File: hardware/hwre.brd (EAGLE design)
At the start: 71.4 x 62.2 mm, 29 parts

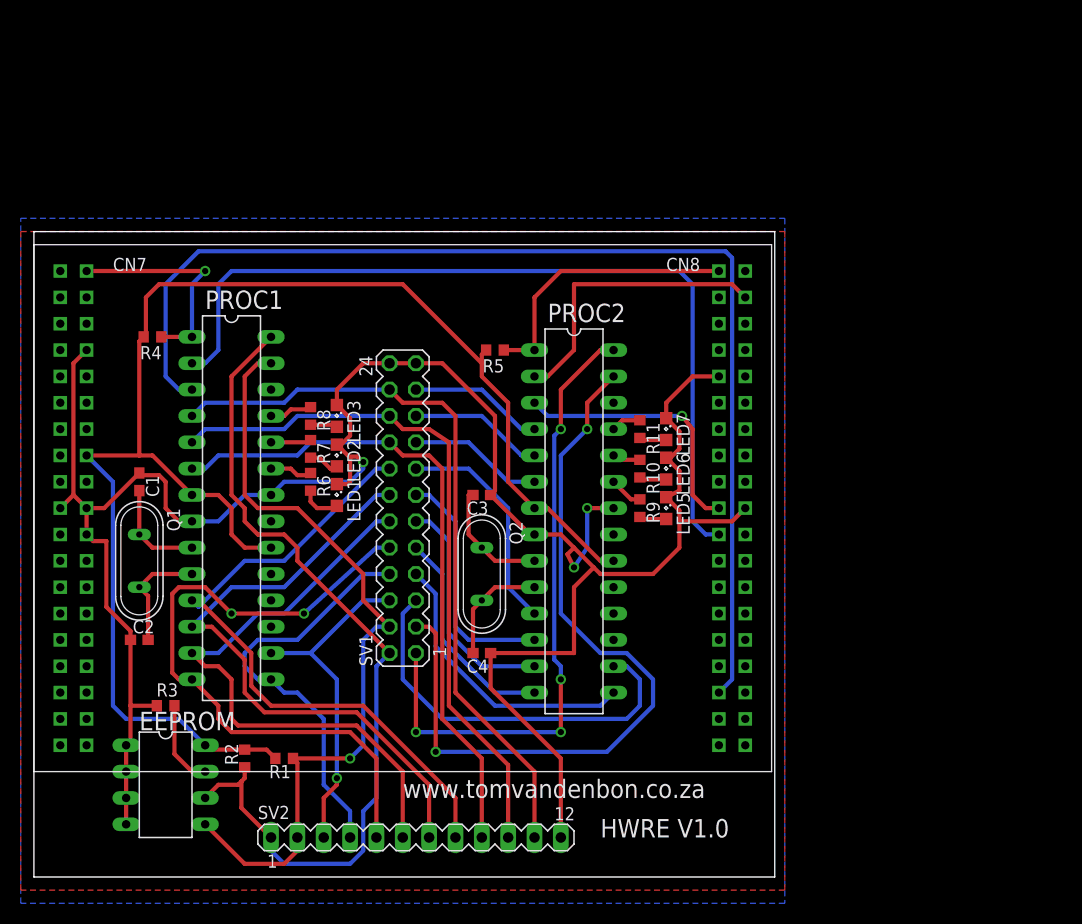
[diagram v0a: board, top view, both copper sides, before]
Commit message: updated pcb to hwre v1.1
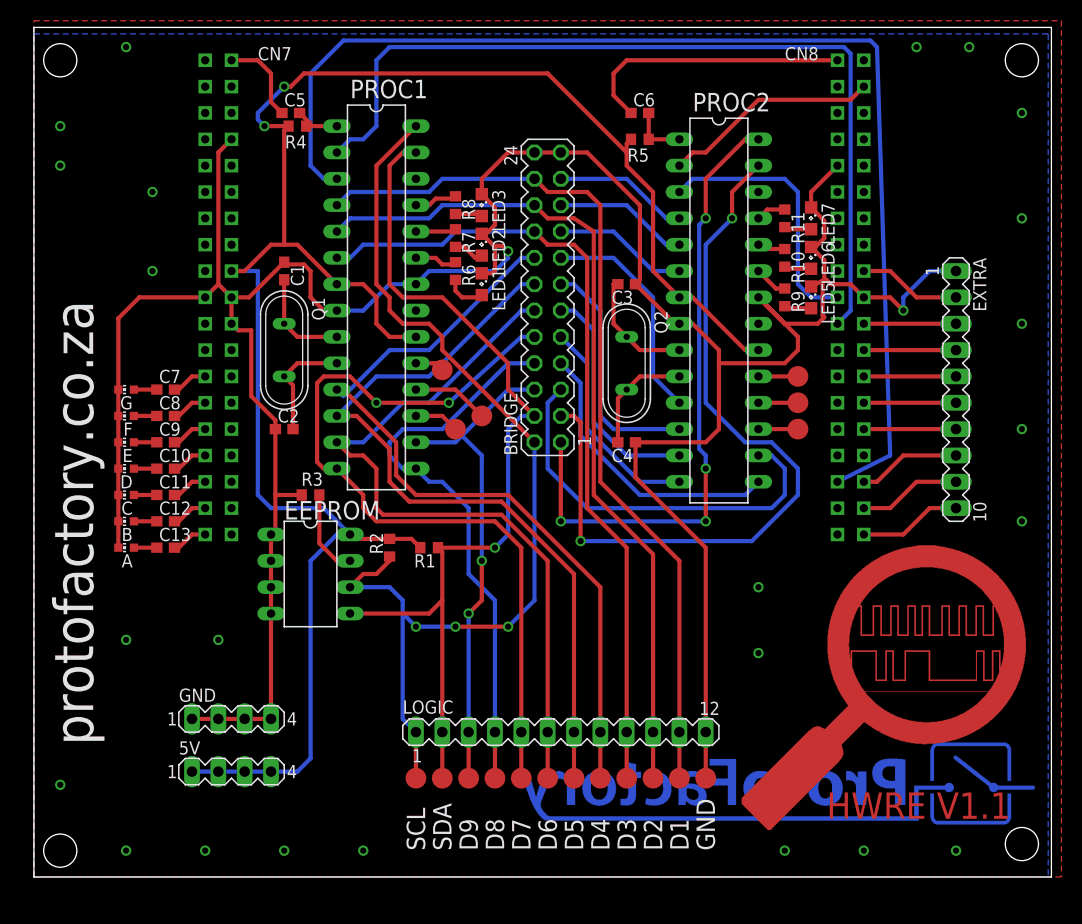
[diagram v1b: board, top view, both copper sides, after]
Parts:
- removed SV1: (no value), con-lstb:MA12-2
- removed SV2: (no value), con-lstb:MA12-1
- added 5V, GND: (no value), con-lstb:MA04-1
- added A, B, C, D, E, F, G: (no value), led:CHIP-LED0603
- added BRIDGE: (no value), con-lstb:MA12-2
- added C10, C11, C12, C13, C5, C6, C7, C8, C9: (no value), rcl:C0603
- added EXTRA: (no value), con-lstb:MA10-1
- added LOGIC: (no value), con-lstb:MA12-1
- added TP1, TP2, TP3, TP4, TP5, TP6: TPTP20R, testpad:TP20R
- added TP10, TP11, TP12, TP13, TP14, TP15, TP16, TP17, TP18, TP7, TP8, TP9: TPSQTP20R, testpad:TP20R
- added U$2: (no value), protofactory:HWRE
- added U$3: (no value), protofactory:LOGO
- C1, C2, C3, C4: value (none) -> 22pF
- Q1, Q2: value (none) -> 8Mhz
- R1, R2: value (none) -> 2k2
- R10, R11, R6, R7, R8, R9: value (none) -> 68E
- R4, R5: value (none) -> 10K
- moved LED5 24.7 mm to (74.9, 55.9)
- moved LED6 24.7 mm to (74.9, 59.7)
- moved LED7 24.7 mm to (74.9, 63.5)
- moved PROC2 24.7 mm to (66.0, 54.6)
- moved R5 24.7 mm to (58.4, 71.1)
- moved EEPROM 24.7 mm to (26.7, 29.2)
- moved PROC1 24.7 mm to (33.0, 55.9)
- moved R1 24.7 mm to (38.1, 31.8)
- moved R3 24.7 mm to (26.7, 36.8)
- moved C1 24.7 mm to (24.1, 58.4)
- moved C2 24.7 mm to (24.1, 43.2)
- moved C3 24.7 mm to (57.1, 57.1)
- moved C4 24.7 mm to (57.1, 41.9)
- moved LED1 24.7 mm to (43.2, 57.1)
- moved LED2 24.7 mm to (43.2, 61.0)
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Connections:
- removed net 3V3: EEPROM.8, PROC1.20, PROC1.7, PROC2.20, PROC2.7, R1.2, R2.2, R4.2, R5.2, U$1.CN7_16
- new net 5V: 5V.1, 5V.2, 5V.3, 5V.4, EEPROM.8, PROC1.20, PROC1.7, PROC2.20, PROC2.7, R1.2, R2.2, R4.2, R5.2, U$1.CN7_18
- new net N$15: PROC1.18, TP2.TP
- new net N$16: PROC1.19, TP3.TP
- new net N$17: PROC2.17, TP4.TP
- new net N$18: PROC2.18, TP5.TP
- new net N$19: PROC2.19, TP6.TP
- new net N$20: C7.2, U$1.CN7_25
- new net N$21: C8.2, U$1.CN7_27
- new net N$22: C9.2, U$1.CN7_29
- new net N$23: C10.2, U$1.CN7_31
- new net N$24: C11.2, U$1.CN7_33
- new net N$25: C12.2, U$1.CN7_35
- new net N$26: C13.2, U$1.CN7_37
- new net N$27: C7.1, G.A
- new net N$28: C8.1, F.A
- new net N$29: C9.1, E.A
- new net N$30: C10.1, D.A
- new net N$31: C.A, C11.1
- new net N$32: B.A, C12.1
- new net N$33: A.A, C13.1
- new net N$34: EXTRA.10, U$1.CN10_38
- new net N$35: EXTRA.9, U$1.CN10_36
- new net N$36: EXTRA.8, U$1.CN10_34
- new net N$37: EXTRA.7, U$1.CN10_30
- new net N$38: EXTRA.6, U$1.CN10_28
- new net N$39: EXTRA.5, U$1.CN10_26
- new net N$40: EXTRA.4, U$1.CN10_24
- new net N$41: EXTRA.3, U$1.CN10_22
- new net N$42: EXTRA.2, U$1.CN10_18
- new net N$8: PROC1.17, TP1.TP
- new net PC6: C5.2, PROC1.1, R4.1
- new net PROC2_PC6: C6.2, PROC2.1, R5.1
- net GND: now also A.C, B.C, BRIDGE.23, BRIDGE.24, C.C, D.C, E.C, EXTRA.1, F.C, G.C, GND.1, GND.2, GND.3, GND.4, LOGIC.12, TP18.TP; no longer SV1.23, SV1.24, SV2.12
- net PROC1_D1: now also BRIDGE.22, LOGIC.11, TP17.TP; no longer SV1.22, SV2.11
- net PROC1_D2: now also BRIDGE.20, LOGIC.10, TP16.TP; no longer SV1.20, SV2.10
- net PROC1_D3: now also BRIDGE.18, LOGIC.9, TP15.TP; no longer SV1.18, SV2.9
- net PROC1_D4: now also BRIDGE.16, LOGIC.8, TP14.TP; no longer SV1.16, SV2.8
- net PROC1_D5: now also BRIDGE.14, LOGIC.7, TP13.TP; no longer SV1.14, SV2.7
- net PROC1_D6: now also BRIDGE.12, LOGIC.6, TP12.TP; no longer SV1.12, SV2.6
- net PROC1_D7: now also BRIDGE.10, LOGIC.5, TP11.TP; no longer SV1.10, SV2.5
- net PROC1_D8: now also BRIDGE.8, LOGIC.4, TP10.TP; no longer SV1.8, SV2.4
- net PROC1_D9: now also BRIDGE.6, LOGIC.3, TP9.TP; no longer SV1.6, SV2.3
- net PROC1_RESET: now also C5.1; no longer PROC1.1, R4.1
- net PROC1_SCL: now also BRIDGE.2, LOGIC.1, TP7.TP; no longer SV1.2, SV2.1
- net PROC1_SDA: now also BRIDGE.4, LOGIC.2, TP8.TP; no longer SV1.4, SV2.2
- net PROC2_D1: now also BRIDGE.21; no longer SV1.21
- net PROC2_D2: now also BRIDGE.19; no longer SV1.19
- net PROC2_D3: now also BRIDGE.17; no longer SV1.17
- net PROC2_D4: now also BRIDGE.15; no longer SV1.15
- net PROC2_D5: now also BRIDGE.13; no longer SV1.13
- net PROC2_D6: now also BRIDGE.11; no longer SV1.11
- net PROC2_D7: now also BRIDGE.9; no longer SV1.9
- net PROC2_D8: now also BRIDGE.7; no longer SV1.7
- net PROC2_D9: now also BRIDGE.5; no longer SV1.5
- net PROC2_RESET: now also C6.1; no longer PROC2.1, R5.1
- net PROC2_SCL: now also BRIDGE.1; no longer SV1.1
- net PROC2_SDA: now also BRIDGE.3; no longer SV1.3
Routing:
- net 5V: track 0.00 -> 185.1 mm, vias 0 -> 2
- net 3V3: track 144.7 -> 0.00 mm
- net GND: track 229.0 -> 296.6 mm, vias 3 -> 26
- net PROC1_D9: track 32.9 -> 47.9 mm, vias 1 -> 2
- net PROC1_D8: track 40.6 -> 55.2 mm
- net PROC1_D7: track 63.8 -> 78.4 mm
- net PROC1_D5: track 60.4 -> 75.0 mm
- net PROC1_D4: track 63.8 -> 78.4 mm
- net PROC1_D6: track 57.9 -> 72.6 mm
- net PROC1_D3: track 63.4 -> 78.0 mm
- net PROC1_D2: track 67.2 -> 81.8 mm
- net PROC1_D1: track 71.3 -> 85.9 mm
- net PROC1_SCL: track 83.4 -> 97.9 mm, vias 0 -> 3
- net PROC1_RESET: track 21.3 -> 8.58 mm, vias 1 -> 0
- net PROC1_SDA: track 75.8 -> 87.6 mm
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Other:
- board size 71.4 x 62.2 mm -> 98.1 x 81.9 mm
- board text added: "D1"
- board text added: "D2"
- board text added: "D3"
- board text added: "D4"
- board text added: "D5"
- board text added: "D6"
- board text added: "D7"
- board text added: "D8"
- board text added: "D9"
- board text added: "GND"
- board text added: "SCL"
- board text added: "SDA"
- board text added: "protofactory.co.za"
- board text added: "tom van den bon July 2014 will hack for beer"
- board text removed: "HWRE V1.0"
- board text removed: "www.tomvandenbon.co.za"
